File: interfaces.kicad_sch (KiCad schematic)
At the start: 33 parts, among them J13 SM04B-SRSS-TB-LF-SN, J14 SM04B-SRSS-TB-LF-SN, J3 SI-51005-F, U7 MAX3051EKA

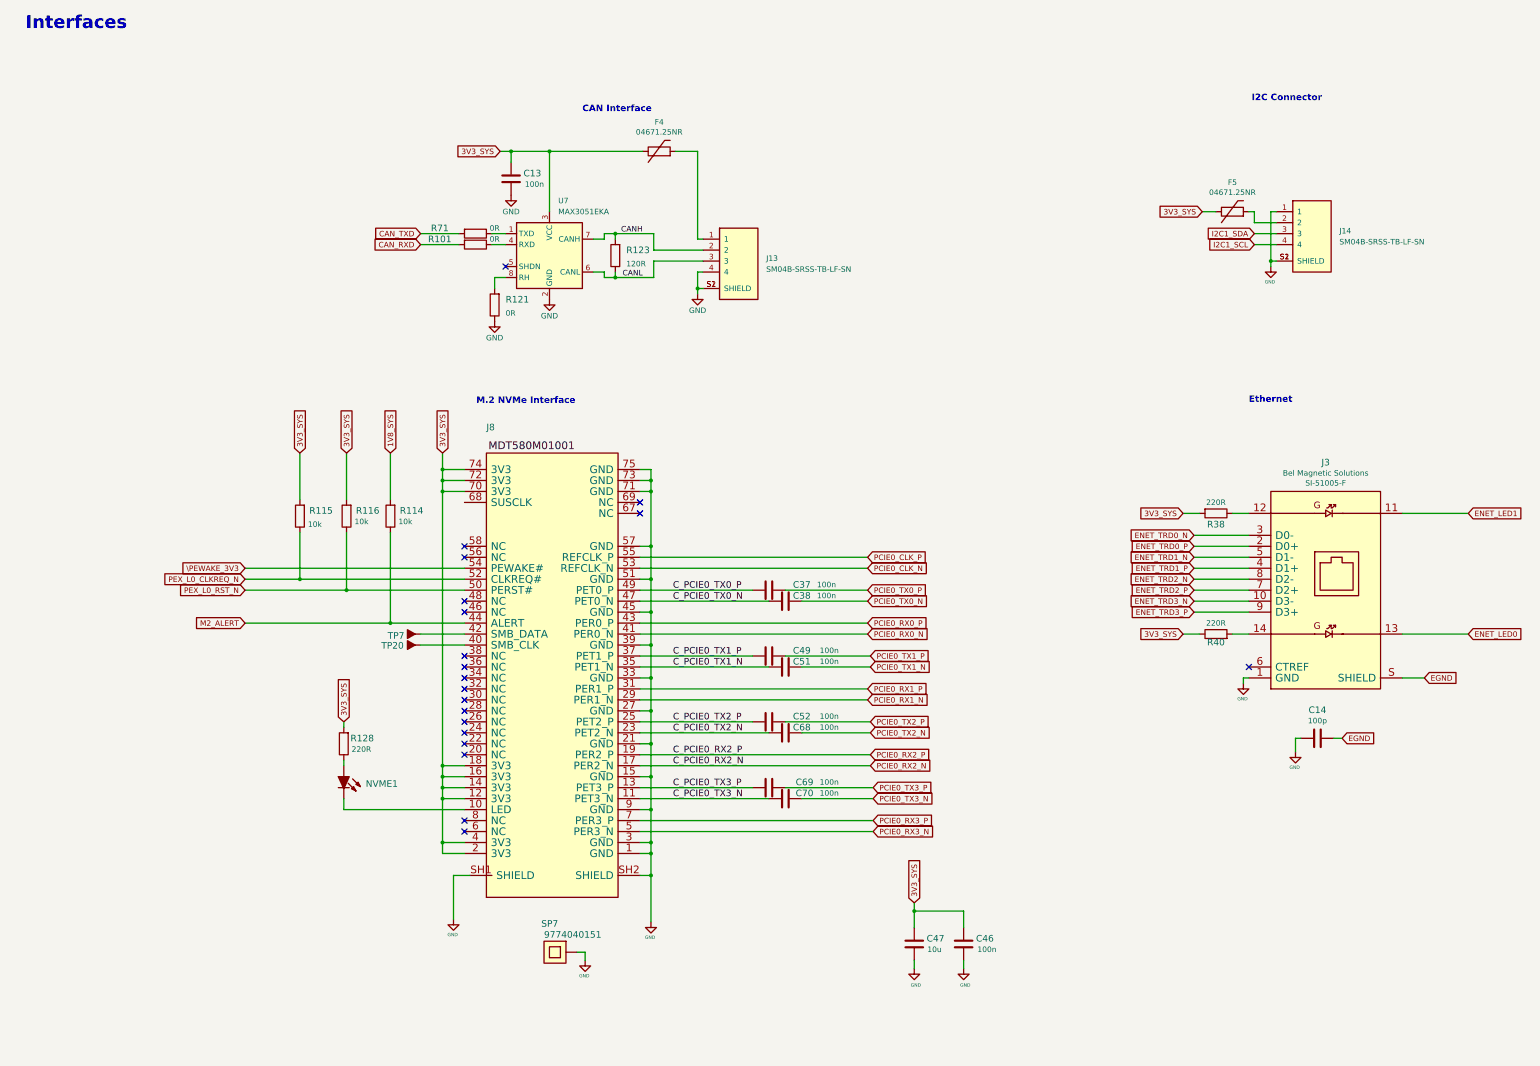
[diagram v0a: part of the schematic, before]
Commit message: WIP: Re-design base board
1. change to more common connector from JLC
2. add WIFI M.2 Key-E connector
3. add USB Hub which contained in nVidia version board
4. change DC connecotor to XT30
5. change USB Mico-B to USB Type C
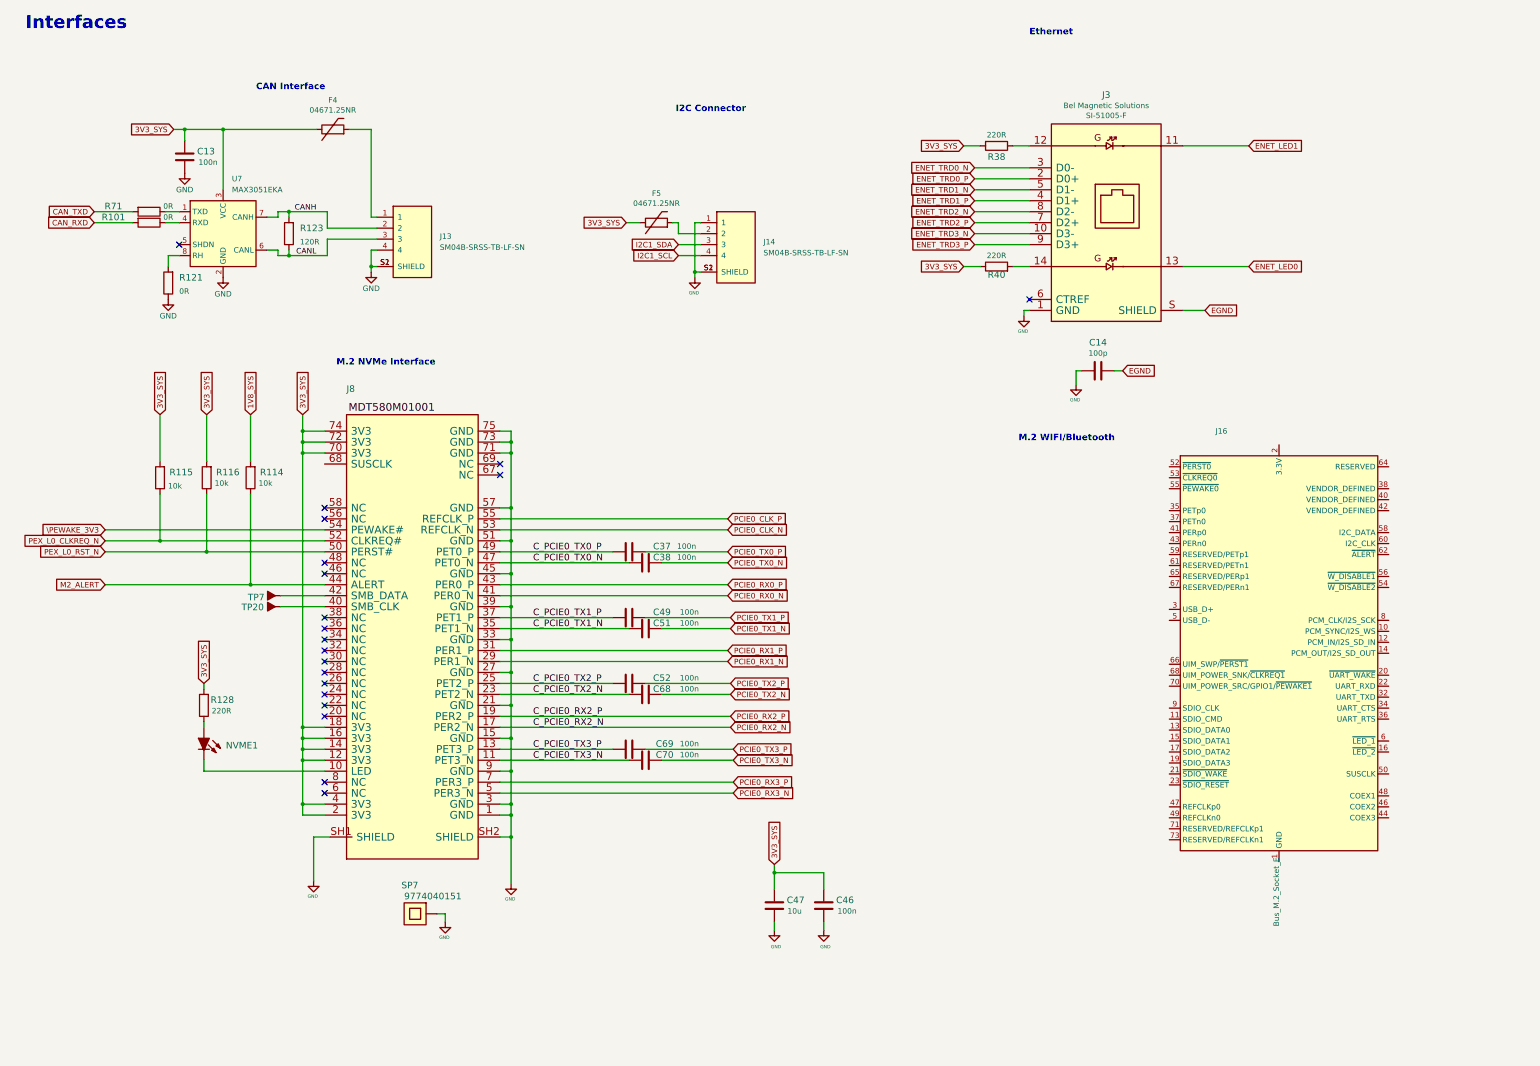
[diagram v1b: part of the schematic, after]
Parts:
- added J16: Bus_M.2_Socket_E, JLC_Footprint:CONN-SMD_APCI0108-P001A, symbol Connector:Bus_M.2_Socket_E
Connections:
- new net: J16.1 (GND), J16.18 (GND), J16.33 (GND), J16.39 (GND), J16.45 (GND), J16.51 (GND), J16.57 (GND), J16.63 (GND), J16.69 (GND), J16.7 (GND), J16.75 (GND)
- new net: J16.2 (3.3V), J16.4 (3.3V), J16.72 (3.3V), J16.74 (3.3V)
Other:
- note added: "M.2 WIFI/Bluetooth"
- moved on the sheet: C13, C14, C37, C38, C46, C47, C49, C51, C52, C68, C69, C70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
